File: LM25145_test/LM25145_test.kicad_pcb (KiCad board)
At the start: 2 copper layers, 40 parts, among them J1 Conn_01x02_Socket, J2 Conn_01x02_Socket

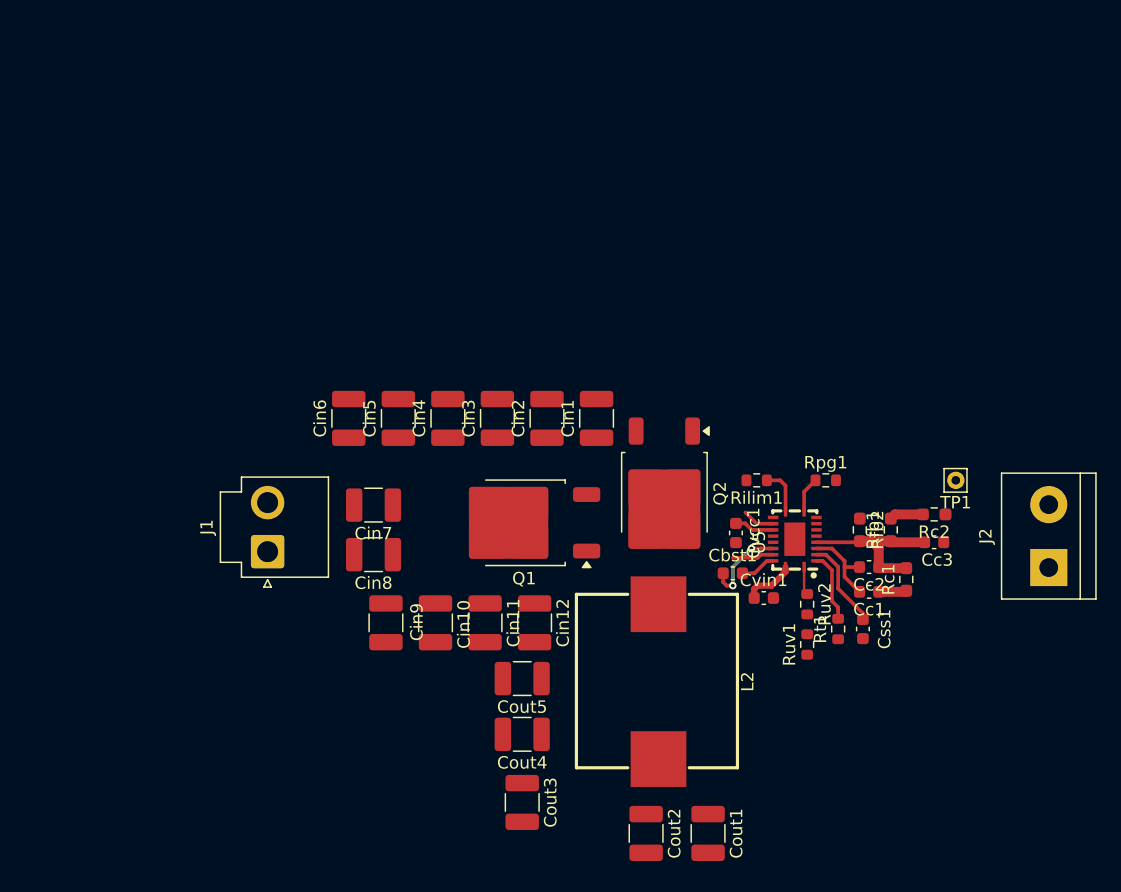
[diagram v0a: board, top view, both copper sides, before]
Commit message: LM25145テスト基板完成、実験用レポートひな形準備
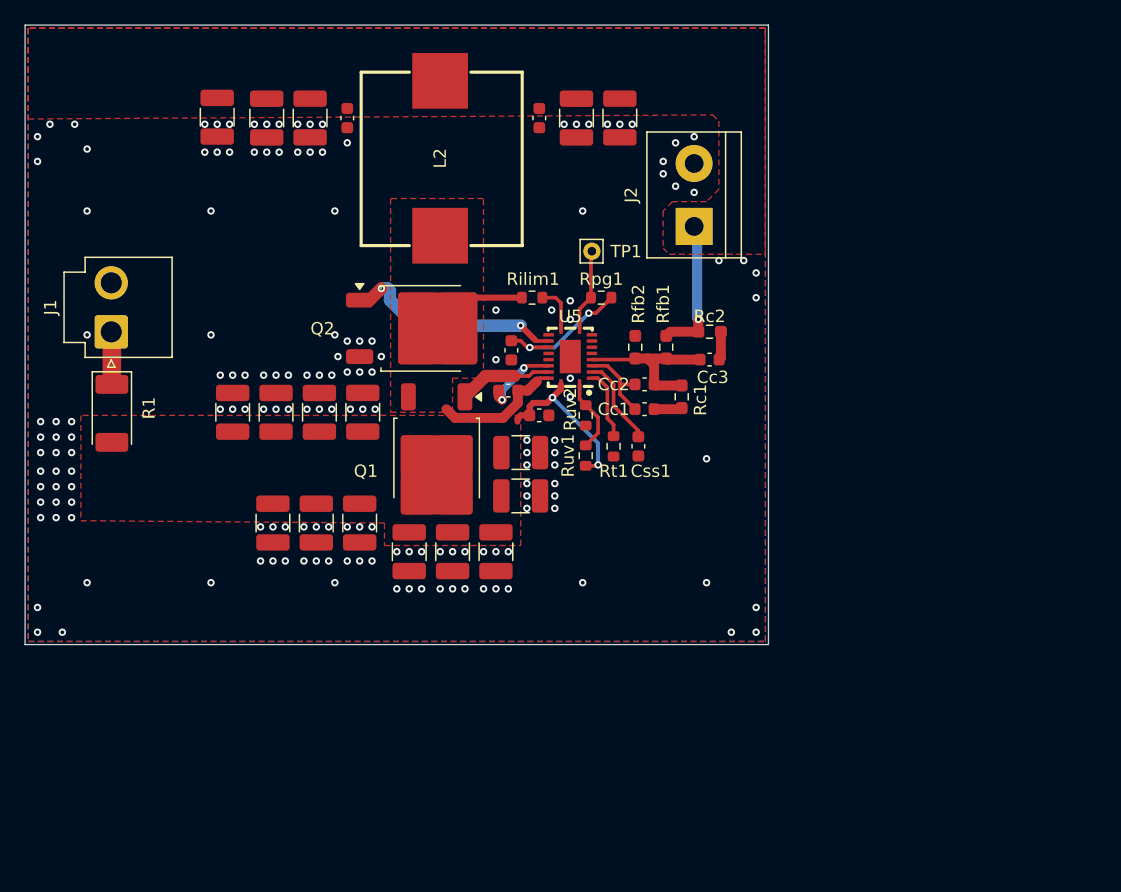
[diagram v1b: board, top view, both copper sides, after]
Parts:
- added Cout1: 100p, Capacitor_SMD:C_0603_1608Metric, F.Cu at (80.9, 45.8)
- added Cout2: 0.1u, Capacitor_SMD:C_0603_1608Metric, F.Cu at (96.4, 45.8)
- added R1: 20m, Diode_SMD:D_2010_5025Metric_Pad1.52x2.65mm_HandSolder, F.Cu at (61.9, 69.6)
- moved Cout3 70.1 mm to (70.4, 45.7)
- moved Cout4 65.4 mm to (74.4, 45.8)
- moved Cout5 57.8 mm to (77.9, 45.8)
- moved Cout6 49.9 mm to (99.4, 45.8), turned to -90 degrees
- moved Cout7 45.9 mm to (102.9, 45.8), turned to -90 degrees
- moved L2 45.8 mm to (88.4, 49.0), turned to 90 degrees
- moved J2 39.7 mm to (108.9, 54.5)
- moved TP1 34.7 mm to (100.6, 56.5)
- moved Cin12 29.7 mm to (71.6, 69.5), turned to 90 degrees
- moved Cin1 27.5 mm to (74.9, 78.4), turned to -90 degrees
- moved Cin11 23.9 mm to (75.1, 69.5), turned to 90 degrees
- moved Q2 23.7 mm to (86.9, 62.7), turned to 0 degrees
- moved Ruv1 23.5 mm to (100.1, 73.0)
- moved Ruv2 23.5 mm to (100.1, 69.8)
- moved Cbst1 23.4 mm to (93.9, 67.8)
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- renumbered Cout1 to Cout3, Cout2 to Cout4, Cout3 to Cout5, Cout4 to Cout6, Cout5 to Cout7
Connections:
- J1 pad 1: GND -> Net-(J1-Pin_1)
- J1 pad 2: +24V -> GND
- J2 pad 1: GND -> +5.1V
- J2 pad 2: +5.1V -> GND
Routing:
- net Net-(Q2-G): track 2.62 -> 17.8 mm, vias 0 -> 2
- net Net-(Q1-S): track 2.89 -> 15.7 mm
- net +24V: track 4.21 -> 13.5 mm, vias 0 -> 2
- net +5.1V: track 2.73 -> 11.4 mm, vias 0 -> 1
- net +7.5V: track 3.22 -> 11.5 mm, vias 0 -> 2
- net Net-(J1-Pin_1): track 0.00 -> 4.26 mm
- net Net-(Q1-G): track 3.36 -> 7.58 mm
- net PGOOD: track 2.88 -> 6.66 mm
- net Net-(U5-EN/UVLO): track 2.28 -> 5.96 mm
- net Net-(Cc3-Pad1): track 0.00 -> 2.31 mm
- net Net-(U5-BST): track 6.99 -> 6.24 mm
- net GND: vias 0 -> 164
- added copper zone on F.Cu, net +24V
- added copper zone on F.Cu, net +5.1V
- added copper zone on B.Cu, net GND
- added copper zone on F.Cu, net GND
- added copper zone on F.Cu, net Net-(Q1-S)
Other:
- board outline added: 60 x 50 mm

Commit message: LM25145_testの基板サイズを小さくして、発注
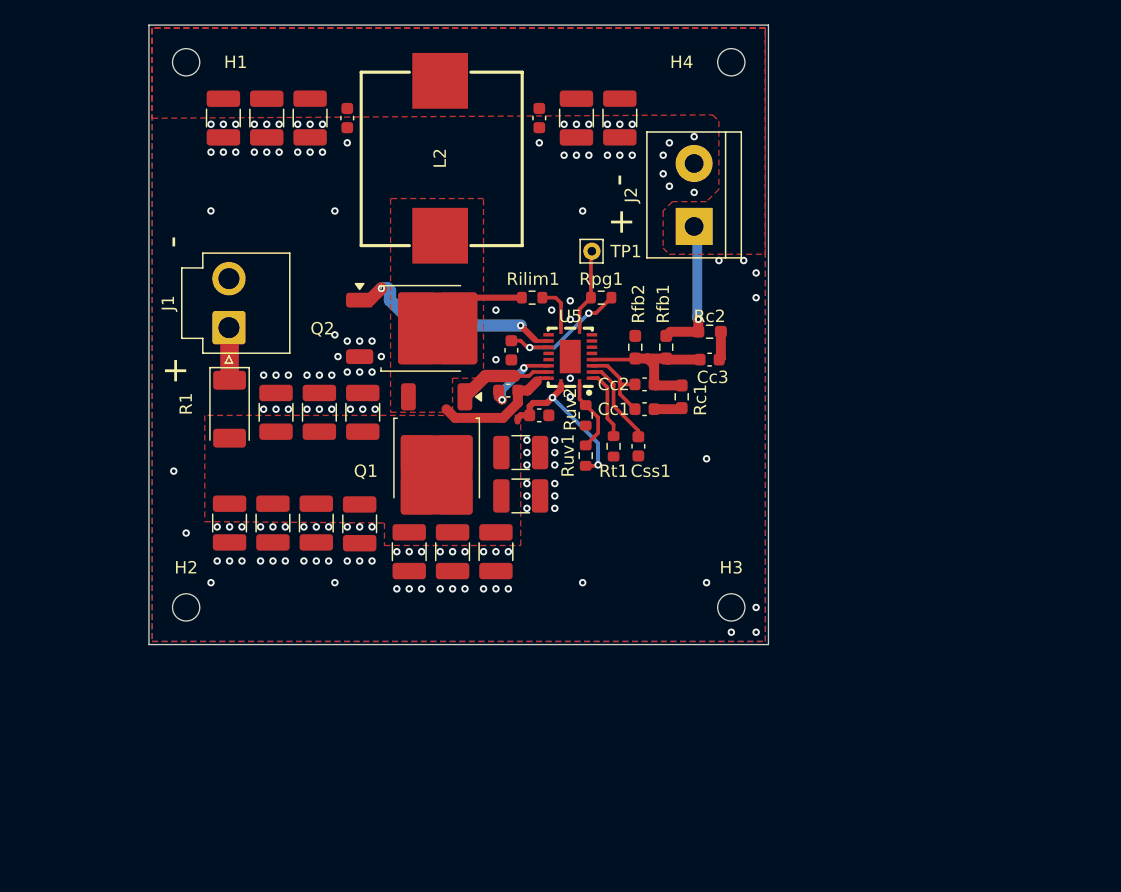
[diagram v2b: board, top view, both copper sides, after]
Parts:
- added H1: MountingHole, MountingHole:MountingHole_2.2mm_M2, F.Cu at (67.9, 41.3)
- added H2: MountingHole, MountingHole:MountingHole_2.2mm_M2, F.Cu at (67.9, 85.3)
- added H3: MountingHole, MountingHole:MountingHole_2.2mm_M2, F.Cu at (111.9, 85.3)
- added H4: MountingHole, MountingHole:MountingHole_2.2mm_M2, F.Cu at (111.9, 41.3)
- moved Cin9 13.2 mm to (94.9, 72.8), turned to 0 degrees
- moved J1 9.51 mm to (71.3, 62.7)
- moved R1 9.51 mm to (71.4, 69.3)
- moved Cin7 4.92 mm to (92.9, 80.8), turned to -90 degrees
- moved Cin4 4.59 mm to (81.9, 78.5)
- moved Cin1 3.50 mm to (71.4, 78.4)
- moved Cin10 3.50 mm to (82.1, 69.5)
- moved Cin11 3.50 mm to (78.6, 69.5)
- moved Cin12 3.50 mm to (75.1, 69.5)
- moved Cin2 3.50 mm to (74.9, 78.4)
- moved Cin3 3.50 mm to (78.4, 78.4)
- moved Cin5 3.50 mm to (85.9, 80.8)
- moved Cin6 3.50 mm to (89.4, 80.8)
- moved Cin8 3.50 mm to (94.9, 76.3)
- moved Cout3 0.50 mm to (70.9, 45.8)
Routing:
- net GND: vias 164 -> 140
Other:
- board size 60 x 50 mm -> 50 x 50 mm
- board text added: "+"
- board text added: "-"

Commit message: 制御基板PCB7割完成
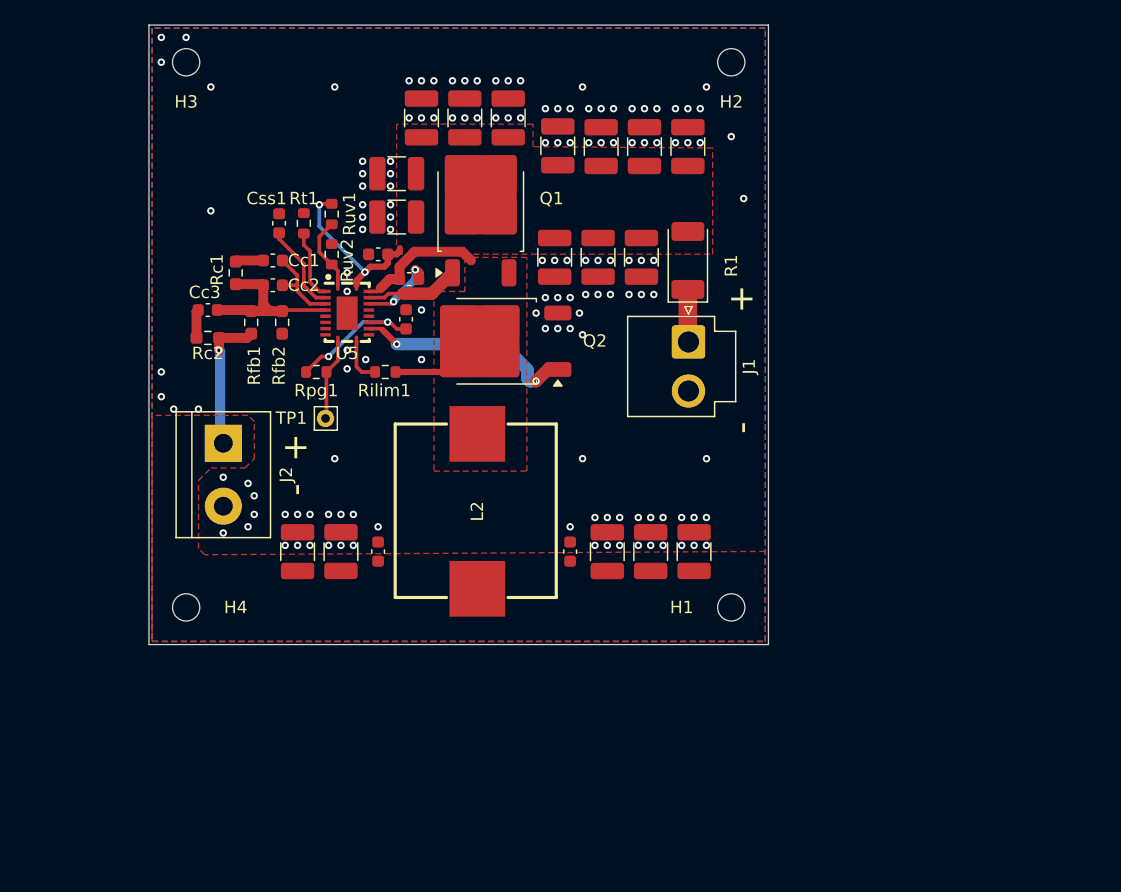
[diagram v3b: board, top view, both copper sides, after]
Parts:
- moved H1 62.2 mm to (111.9, 85.3), turned to 180 degrees
- moved H2 62.2 mm to (111.9, 41.3), turned to 180 degrees
- moved H3 62.2 mm to (67.9, 41.3), turned to 180 degrees
- moved H4 62.2 mm to (67.9, 85.3), turned to 180 degrees
- moved Cout3 51.6 mm to (108.9, 80.8), turned to 90 degrees
- moved Cin1 47.9 mm to (108.4, 48.1), turned to 90 degrees
- moved Cout4 46.7 mm to (105.4, 80.8), turned to 90 degrees
- moved Cout7 43.6 mm to (76.9, 80.8), turned to 90 degrees
- moved Cin2 42.7 mm to (104.9, 48.1), turned to 90 degrees
- moved Cout5 42.4 mm to (101.9, 80.8), turned to 90 degrees
- moved J2 41.8 mm to (70.9, 72.0), turned to -90 degrees
- moved Cc3 40.7 mm to (69.6, 61.3), turned to 0 degrees
- moved Rc2 40.5 mm to (69.6, 63.5), turned to 0 degrees
- moved Cout6 39.8 mm to (80.4, 80.8), turned to 90 degrees
- moved Cout1 39.3 mm to (98.9, 80.8), turned to -90 degrees
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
